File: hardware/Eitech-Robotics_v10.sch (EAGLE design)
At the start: 144 parts, among them IC1 ATSAMW25-MR510PB, IC2 74LVC244PW, IC3 A3909-LY, IC4 A3909-LY, IC5 VREG-TS1117CW-3V3, IC6 AP65200-SP, J1 JST3-B3B-PH-K, J2 JST3-B3B-PH-K, J3 JST3-B3B-PH-K, J4 JST3-B3B-PH-K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

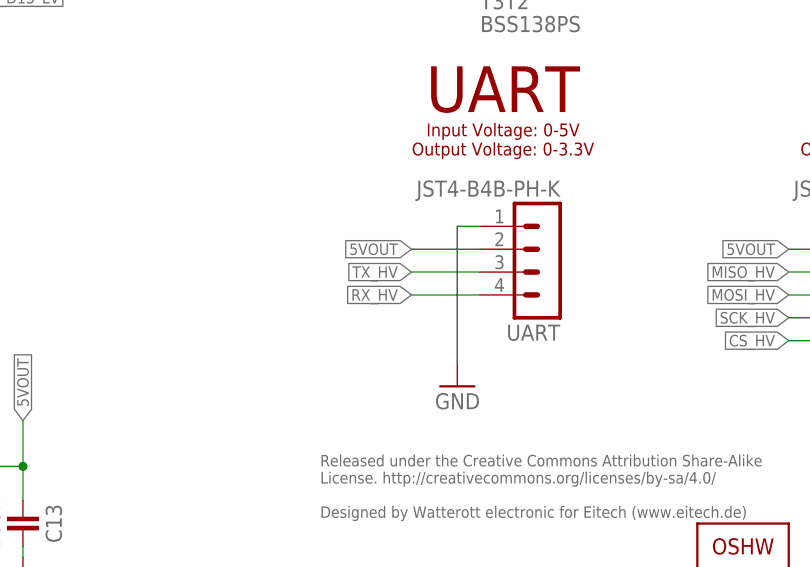
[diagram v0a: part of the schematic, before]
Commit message: updated schematics
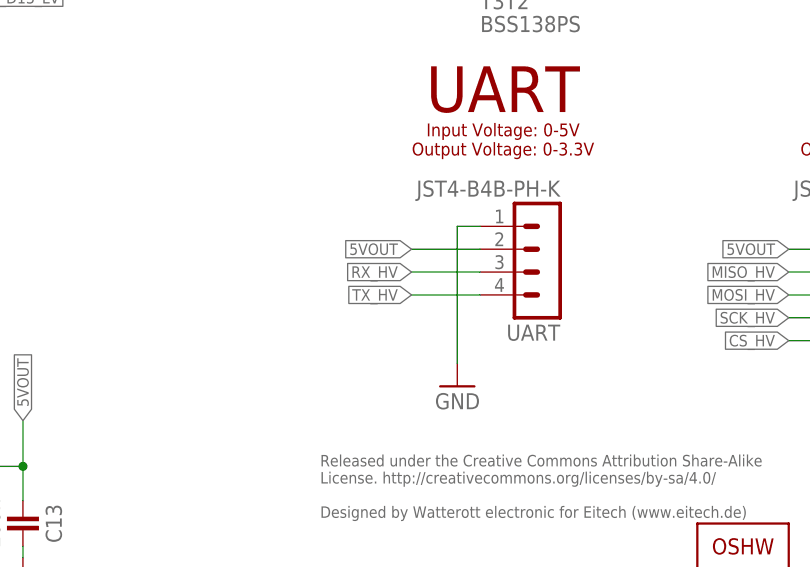
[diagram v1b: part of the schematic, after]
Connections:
- net RX_HV: now also UART.3; no longer UART.4
- net TX_HV: now also UART.4; no longer UART.3
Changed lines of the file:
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@@
 <layer number="51" name="tDocu" color="7" fill="1" visible="no" active="no"/>
 <layer number="52" name="bDocu" color="7" fill="1" visible="no" active="no"/>
-<layer number="53" name="tGND_GNDA" color="7" fill="9" visible="no" active="no"/>
-<layer number="54" name="bGND_GNDA" color="1" fill="9" visible="no" active="no"/>
-<layer number="56" name="wert" color="7" fill="1" visible="no" active="no"/>
-<layer number="57" name="tCAD" color="7" fill="1" visible="no" active="no"/>
-<layer number="60" name="Board" color="7" fill="1" visible="no" active="no"/>
 <layer number="90" name="Modules" color="5" fill="1" visible="yes" active="yes"/>
 <layer number="91" name="Nets" color="2" fill="1" visible="yes" active="yes"/>
@@
 <layer number="98" name="Guide" color="6" fill="1" visible="yes" active="yes"/>
 <layer number="99" name="SpiceOrder" color="5" fill="1" visible="yes" active="yes"/>
-<layer number="100" name="Muster" color="7" fill="1" visible="no" active="no"/>
-<layer number="105" name="Beschreib" color="9" fill="1" visible="no" active="no"/>
-<layer number="106" name="BGA-Top" color="4" fill="1" visible="no" active="no"/>
-<layer number="107" name="BD-Top" color="5" fill="1" visible="no" active="no"/>
-<layer number="153" name="FabDoc1" color="6" fill="1" visible="no" active="no"/>
-<layer number="154" name="FabDoc2" color="2" fill="1" visible="no" active="no"/>
-<layer number="155" name="FabDoc3" color="7" fill="15" visible="no" active="no"/>
-<layer number="200" name="200bmp" color="1" fill="10" visible="no" active="no"/>
-<layer number="217" name="217bmp" color="18" fill="1" visible="no" active="no"/>
-<layer number="218" name="218bmp" color="19" fill="1" visible="no" active="no"/>
-<layer number="219" name="219bmp" color="20" fill="1" visible="no" active="no"/>
-<layer number="220" name="220bmp" color="21" fill="1" visible="no" active="no"/>
-<layer number="221" name="221bmp" color="22" fill="1" visible="no" active="no"/>
-<layer number="222" name="222bmp" color="23" fill="1" visible="no" active="no"/>
-<layer number="223" name="223bmp" color="24" fill="1" visible="no" active="no"/>
-<layer number="224" name="224bmp" color="25" fill="1" visible="no" active="no"/>
-<layer number="250" name="Descript" color="3" fill="1" visible="no" active="no"/>
-<layer number="251" name="SMDround" color="12" fill="11" visible="no" active="no"/>
 </layers>
 <schematic xreflabel="%F%N/%S.%C%R" xrefpart="/%S.%C%R">
@@
 <net name="RX_HV" class="0">
 <segment>
-<label x="299.72" y="40.64" size="1.27" layer="95" rot="R180" xref="yes"/>
-<wire x1="307.34" y1="40.64" x2="299.72" y2="40.64" width="0.1524" layer="91"/>
-<pinref part="UART" gate="J" pin="4"/>
+<label x="299.72" y="43.18" size="1.27" layer="95" rot="R180" xref="yes"/>
+<wire x1="307.34" y1="43.18" x2="299.72" y2="43.18" width="0.1524" layer="91"/>
+<pinref part="UART" gate="J" pin="3"/>
 </segment>
 <segment>
@@
 <net name="TX_HV" class="0">
 <segment>
-<wire x1="299.72" y1="43.18" x2="307.34" y2="43.18" width="0.1524" layer="91"/>
-<label x="299.72" y="43.18" size="1.27" layer="95" rot="R180" xref="yes"/>
-<pinref part="UART" gate="J" pin="3"/>
-</segment>
-<segment>
+<wire x1="299.72" y1="40.64" x2="307.34" y2="40.64" width="0.1524" layer="91"/>
+<label x="299.72" y="40.64" size="1.27" layer="95" rot="R180" xref="yes"/>
+<pinref part="UART" gate="J" pin="4"/>
+</segment>
+<segment>
